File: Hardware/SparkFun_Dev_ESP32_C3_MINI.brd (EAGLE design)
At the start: 21 x 33.3 mm, 88 parts, among them J1 USB Female Type C Connector, J5 Vertical Qwiic Connector, U1 ESP32-C3_MINI-1, U2 RT9080-33GJ5

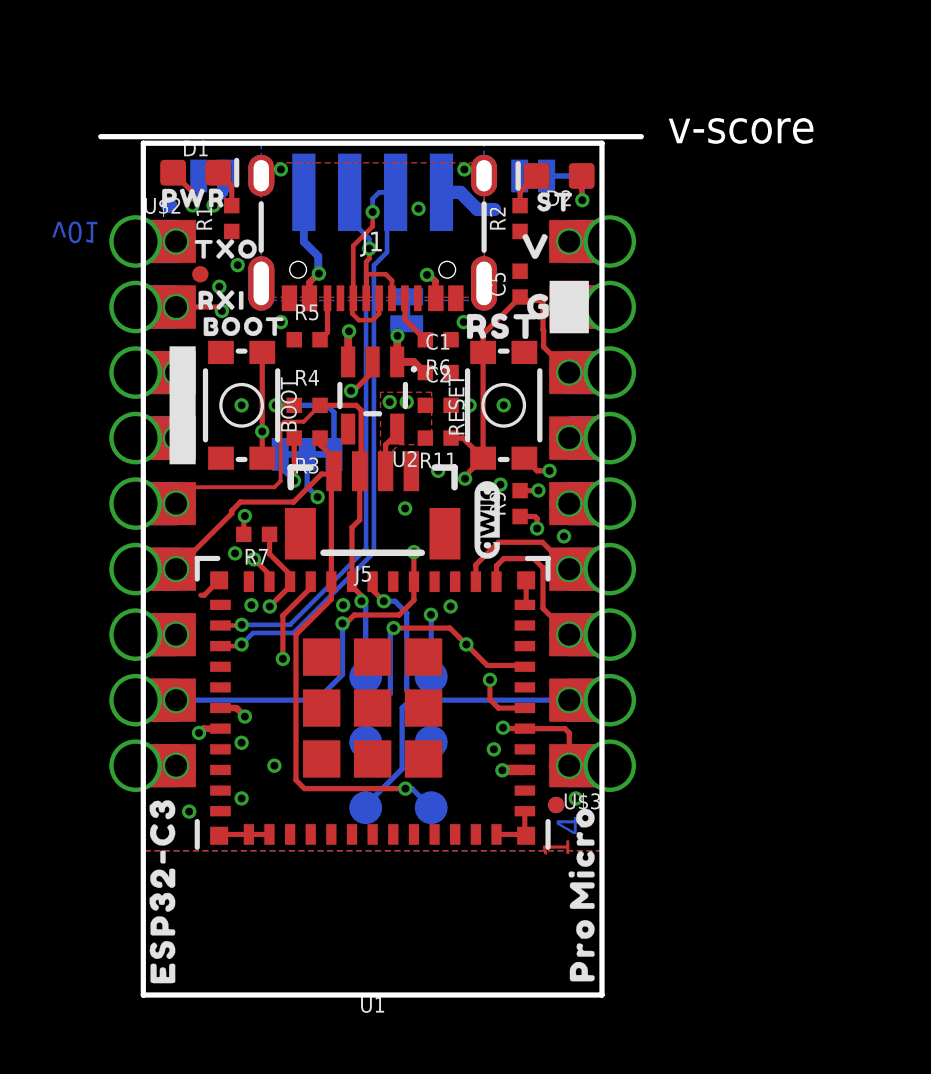
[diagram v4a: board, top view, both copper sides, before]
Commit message: Adds more aesthetic changes
* Note on previous commit: I2C labels were removed from silk
* Fixes ground silk rectangle
* rotates qwiic label
* Shrinks VBUS polygon
* Moves boot capacitor to other side of button
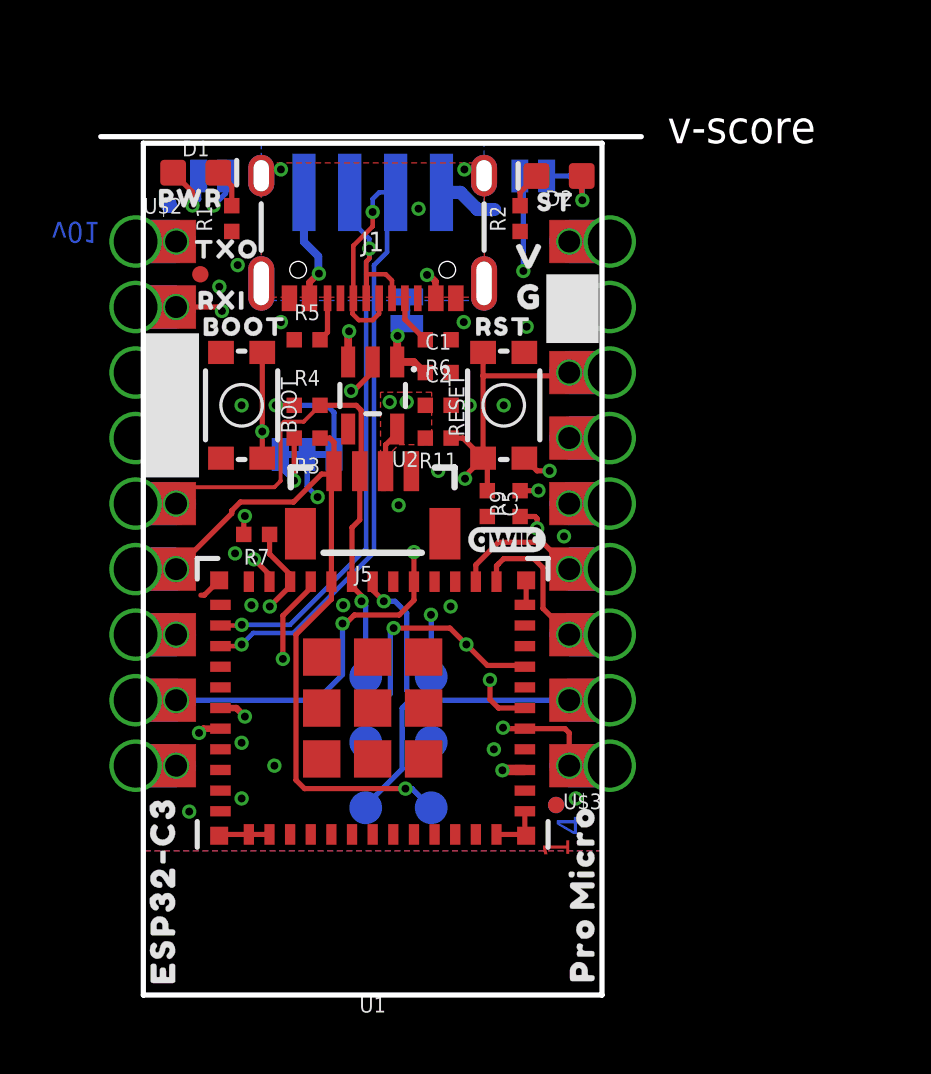
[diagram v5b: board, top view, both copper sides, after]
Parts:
- removed LOGO2: QWIIC_LOGO_3MM, SparkFun-Aesthetics:QWIIC_3MM
- added U$50: (no value), SparkFun-Aesthetics:QWIIC_3MM
- moved C5 8.60 mm to (14.6, 19.1), turned to 270 degrees
- moved U$39 0.54 mm to (16.3, 27.1)
- moved U$38 0.46 mm to (16.3, 28.6)
- moved U$26 0.16 mm to (9.25, 28.6)
- moved U$25 0.13 mm to (11.0, 28.6)
- moved U$44 0.13 mm to (3.10, 30.9)
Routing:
- net IO10/I2S_FS: track 14.5 -> 30.9 mm, vias 2 -> 3
- net !RESET!: track 30.9 -> 28.8 mm
- net GND: vias 21 -> 22

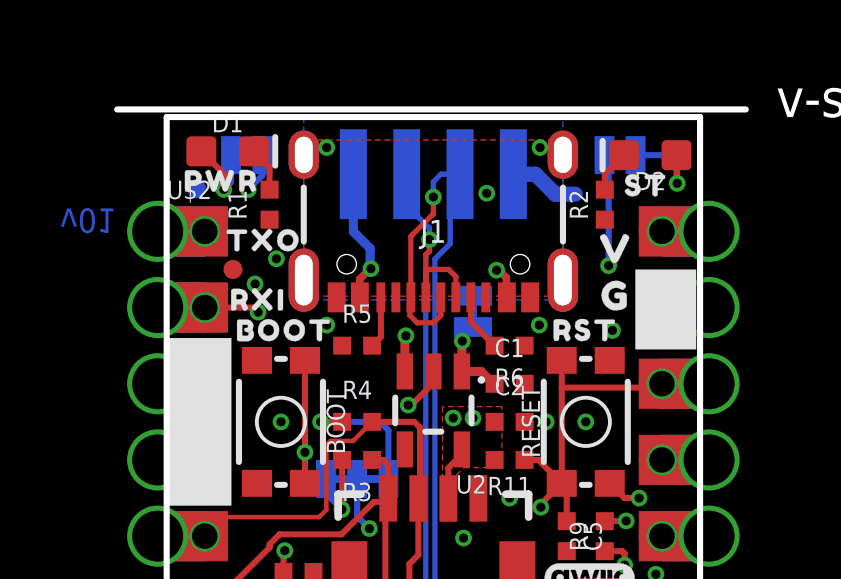
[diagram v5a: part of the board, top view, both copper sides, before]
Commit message: Fixes DRC issues
* Moves shield jumper away from VUSB via
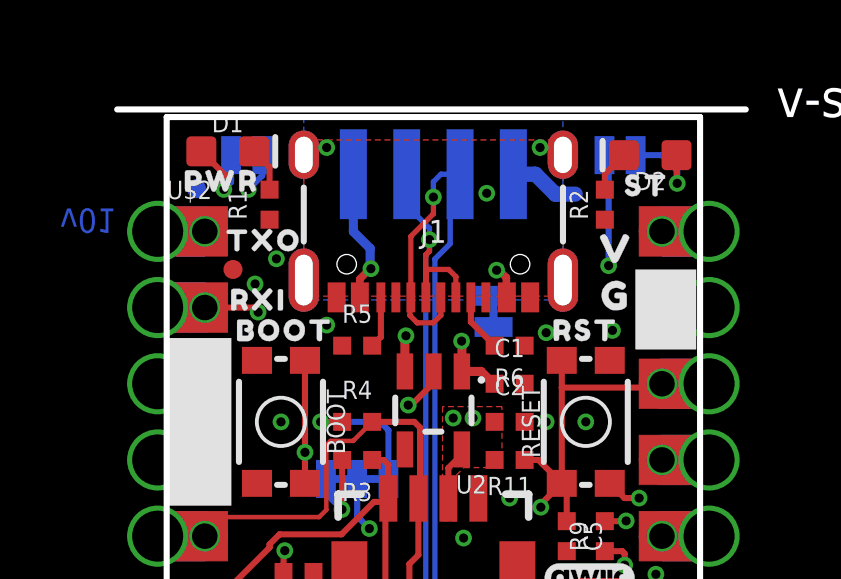
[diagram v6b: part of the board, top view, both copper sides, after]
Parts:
- moved SHLD 0.69 mm to (12.2, 26.5)
- moved U$9 0.60 mm to (14.0, 26.2)
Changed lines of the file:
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@@
 <attribute name="VALUE" x="7.62" y="19.812" size="0.6096" layer="28" font="vector" ratio="20" rot="MR0" align="top-center"/>
 </element>
-<element name="SHLD" library="SparkFun-Jumpers" package="SMT-JUMPER_2_NC_TRACE_SILK" package3d_urn="urn:adsk.eagle:package:39281/1" value="JUMPER-SMT_2_NC_TRACE_SILK" x="11.4808" y="26.543" smashed="yes" rot="MR270">
-<attribute name="NAME" x="10.3378" y="26.543" size="0.6096" layer="26" font="vector" ratio="20" rot="MR270" align="bottom-center"/>
-<attribute name="VALUE" x="12.6238" y="26.543" size="0.6096" layer="28" font="vector" ratio="20" rot="MR270" align="top-center"/>
+<element name="SHLD" library="SparkFun-Jumpers" package="SMT-JUMPER_2_NC_TRACE_SILK" package3d_urn="urn:adsk.eagle:package:39281/1" value="JUMPER-SMT_2_NC_TRACE_SILK" x="12.1666" y="26.543" smashed="yes" rot="MR270">
+<attribute name="NAME" x="11.0236" y="26.543" size="0.6096" layer="26" font="vector" ratio="20" rot="MR270" align="bottom-center"/>
+<attribute name="VALUE" x="13.3096" y="26.543" size="0.6096" layer="28" font="vector" ratio="20" rot="MR270" align="top-center"/>
 </element>
 <element name="R5" library="SparkFun-Resistors" package="0402-TIGHT" value="5.1k" x="7.62" y="25.4" smashed="yes">
@@
 <element name="U$31" library="prod" package="G36" value="" x="12.827" y="28.956" smashed="yes" rot="MR270"/>
 <element name="U$32" library="prod" package="V35" value="" x="7.493" y="28.956" smashed="yes" rot="MR270"/>
-<element name="U$9" library="prod" package="#SH#44" value="" x="13.462" y="26.035" smashed="yes" rot="MR0"/>
+<element name="U$9" library="prod" package="#SH#44" value="" x="14.0462" y="26.1874" smashed="yes" rot="MR0"/>
 <element name="U$33" library="prod" package="G36" value="" x="13.589" y="9.779" smashed="yes" rot="MR0"/>
 <element name="U$34" library="prod" package="ESP32#C32" value="" x="10.16" y="5.08" smashed="yes" rot="MR0"/>
@@
 <wire x1="3.6348" y1="15.5" x2="3.5" y2="15.5" width="0.2" layer="1"/>
 <via x="6.604" y="26.0858" extent="1-16" drill="0.3048"/>
-<via x="13.6906" y="26.0858" extent="1-16" drill="0.3048"/>
+<via x="13.9192" y="25.8318" extent="1-16" drill="0.3048"/>
 <via x="4.2164" y="27.4574" extent="1-16" drill="0.3048"/>
 <via x="18.034" y="7.62" extent="1-16" drill="0.3048"/>
@@
 <vertex x="7.5438" y="27.559"/>
 </polygon>
-<wire x1="11.11" y1="24.5411" x2="11.11" y2="25.5372" width="0.3048" layer="1"/>
-<wire x1="11.11" y1="25.5372" x2="11.1252" y2="25.5524" width="0.3048" layer="1"/>
-<via x="11.1252" y="25.5524" extent="1-16" drill="0.3048"/>
+<wire x1="11.11" y1="24.5411" x2="11.11" y2="25.5422" width="0.3048" layer="1"/>
+<wire x1="11.11" y1="25.5422" x2="11.0998" y2="25.5524" width="0.3048" layer="1"/>
+<via x="11.0998" y="25.5524" extent="1-16" drill="0.3048"/>
 <wire x1="9.21" y1="24.5411" x2="9.21" y2="25.6946" width="0.3048" layer="1"/>
 <wire x1="9.21" y1="25.6946" x2="9.2456" y2="25.7302" width="0.3048" layer="1"/>
@@
 <contactref element="D1" pad="A"/>
 <contactref element="PWR" pad="1"/>
-<wire x1="3.4163" y1="31.75" x2="3.4163" y2="31.3817" width="0.2032" layer="16"/>
 <via x="3.175" y="30.607" extent="1-16" drill="0.3048"/>
 <wire x1="3.175" y1="30.607" x2="3.175" y2="31.127" width="0.2032" layer="1"/>

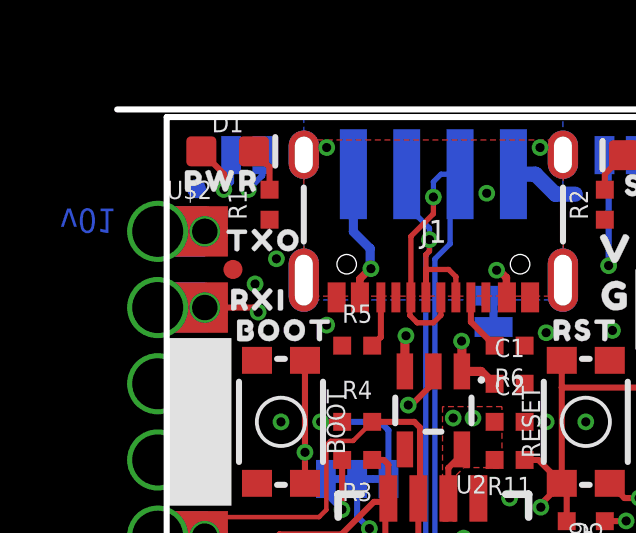
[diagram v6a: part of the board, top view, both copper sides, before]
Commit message: Moves version onto the PCB, and rolls version in schematic
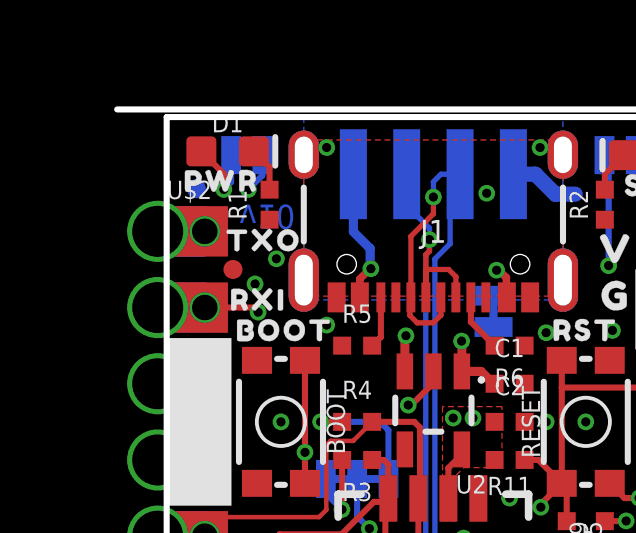
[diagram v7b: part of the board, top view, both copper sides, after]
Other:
- board text added: "v10"
- board text removed: "v01"
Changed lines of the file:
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@@
 <setting verticaltext="up"/>
 </settings>
-<grid distance="0.05" unitdist="inch" unit="inch" style="dots" multiple="1" display="yes" altdistance="0.001" altunitdist="inch" altunit="inch"/>
+<grid distance="0.05" unitdist="inch" unit="inch" style="dots" multiple="1" display="yes" altdistance="0.005" altunitdist="inch" altunit="inch"/>
 <layers>
 <layer number="1" name="Top" color="4" fill="1" visible="yes" active="yes"/>
@@
 <dimension x1="15.24" y1="22.86" x2="19.05" y2="22.86" x3="17.145" y3="36.449" textsize="1.016" textratio="15" layer="47" unit="inch"/>
 <dimension x1="5.08" y1="22.86" x2="1.27" y2="22.86" x3="3.175" y3="36.449" textsize="0.9652" textratio="15" layer="47" unit="inch"/>
-<text x="-2.286" y="29.972" size="0.8128" layer="16" font="vector" ratio="20" rot="SMR180">v01</text>
+<text x="3.683" y="30.099" size="0.8128" layer="16" font="vector" ratio="20" rot="SMR180">v10</text>
 <wire x1="-0.381" y1="33.274" x2="20.574" y2="33.274" width="0.2032" layer="46"/>
 <text x="21.59" y="33.02" size="1.27" layer="46" font="vector" ratio="15">v-score</text>
@@
 <element name="FRAME2" library="SparkFun-Aesthetics" package="CREATIVE_COMMONS" value="FRAME-LEDGER" x="-11.43" y="-25.4" smashed="yes">
 <attribute name="DESIGNER" value="Elias Santistevan" x="-11.43" y="-25.4" size="1.778" layer="27" font="vector" ratio="15" display="off"/>
-<attribute name="REV" value="v01" x="-11.43" y="-25.4" size="1.778" layer="27" font="vector" ratio="15" display="off"/>
+<attribute name="REV" value="v10" x="-11.43" y="-25.4" size="1.778" layer="27" font="vector" ratio="15" display="off"/>
 </element>
 <element name="D2" library="SparkFun-LED" package="LED-0603" value="Blue" x="17.387" y="31.75" smashed="yes" rot="R180">

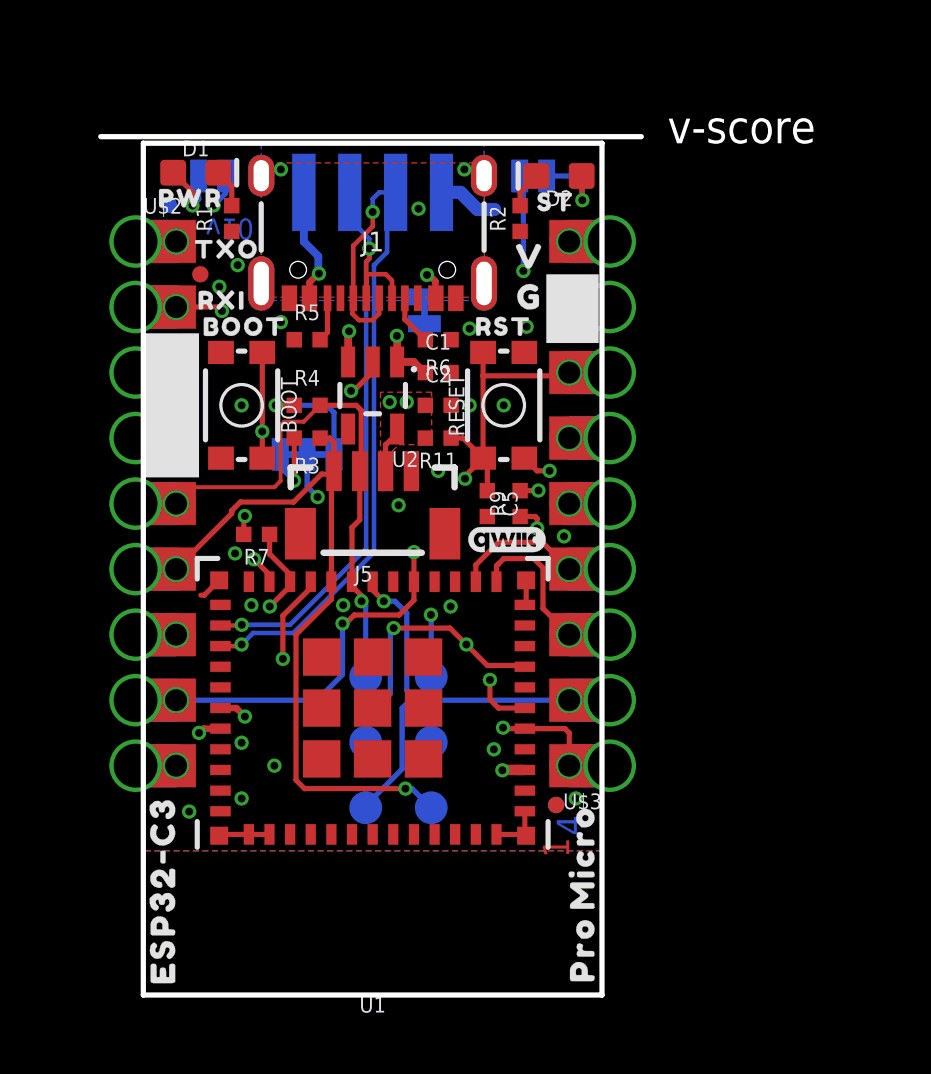
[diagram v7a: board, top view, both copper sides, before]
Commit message: Fixes some acid traps, fixes some schematic odds and ends
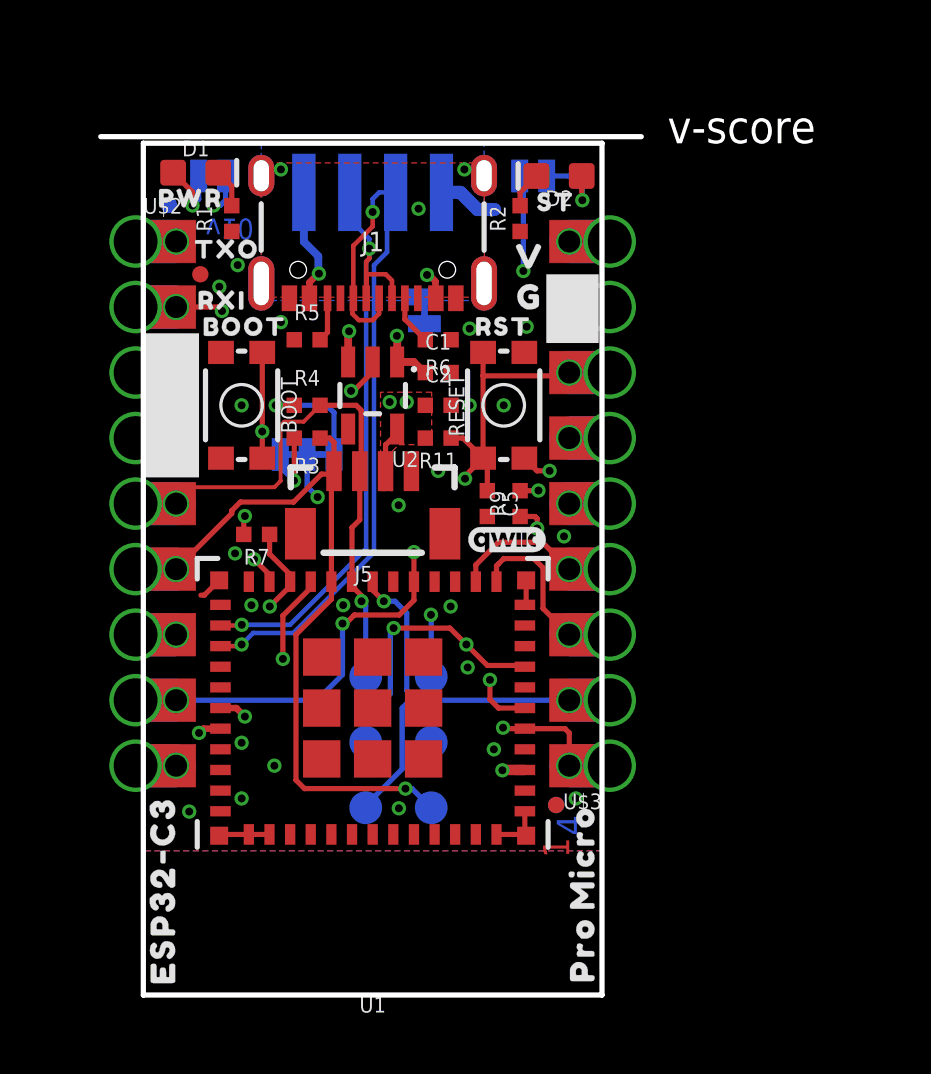
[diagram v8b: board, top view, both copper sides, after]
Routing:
- net GND: vias 22 -> 24
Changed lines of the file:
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@@
 <layer number="45" name="Holes" color="7" fill="1" visible="yes" active="yes"/>
 <layer number="46" name="Milling" color="3" fill="1" visible="no" active="yes"/>
-<layer number="47" name="Measures" color="7" fill="1" visible="no" active="yes"/>
+<layer number="47" name="Measures" color="7" fill="1" visible="yes" active="yes"/>
 <layer number="48" name="Document" color="7" fill="1" visible="no" active="yes"/>
 <layer number="49" name="Reference" color="13" fill="1" visible="yes" active="yes"/>
@@
 <wire x1="7.62" y1="19.7104" x2="8.0264" y2="19.304" width="0.2032" layer="16"/>
 <via x="8.0264" y="19.304" extent="1-16" drill="0.3048"/>
-<wire x1="4.4577" y1="31.75" x2="4.4577" y2="31.0721" width="0.2032" layer="16"/>
-<wire x1="4.4577" y1="31.0721" x2="3.9926" y2="30.607" width="0.2032" layer="16"/>
+<wire x1="4.4577" y1="31.75" x2="4.4577" y2="30.8181" width="0.2032" layer="16"/>
+<wire x1="4.4577" y1="30.8181" x2="4.2466" y2="30.607" width="0.2032" layer="16"/>
+<wire x1="4.2466" y1="30.607" x2="3.9926" y2="30.607" width="0.2032" layer="16"/>
 <via x="3.9926" y="30.607" extent="1-16" drill="0.3048"/>
 </signal>
@@
 <wire x1="16.53" y1="20.32" x2="17.018" y2="20.32" width="0.2032" layer="1"/>
 <via x="16.129" y="25.908" extent="1-16" drill="0.3048"/>
+<via x="11.176" y="7.239" extent="1-16" drill="0.3048"/>
+<via x="13.843" y="12.7" extent="1-16" drill="0.3048"/>
 </signal>
 <signal name="N$4">
@@
 <wire x1="7.493" y1="31.115" x2="7.493" y2="29.19959375" width="0.3048" layer="16"/>
 <wire x1="7.493" y1="29.19959375" x2="8.0522" y2="28.64039375" width="0.3048" layer="16"/>
-<wire x1="17.78" y1="29.21" x2="12.192" y2="29.21" width="0.508" layer="2"/>
-<wire x1="12.192" y1="29.21" x2="10.922" y2="27.94" width="0.508" layer="2"/>
+<wire x1="11.43" y1="28.956" x2="11.43" y2="28.067" width="0.508" layer="2"/>
+<wire x1="17.78" y1="29.21" x2="11.684" y2="29.21" width="0.508" layer="2"/>
+<wire x1="11.684" y1="29.21" x2="11.43" y2="28.956" width="0.508" layer="2"/>
 <wire x1="17.78" y1="29.21" x2="19.35" y2="29.21" width="0" layer="19" extent="1-1"/>
+<wire x1="12.2678" y1="27.9146" x2="11.43" y2="28.067" width="0" layer="19" extent="1-2"/>
+<wire x1="11.0998" y1="25.5524" x2="12.61" y2="27.01" width="0" layer="19" extent="1-1"/>
+<wire x1="9.2456" y1="25.7302" x2="11.0998" y2="25.5524" width="0" layer="19" extent="1-1"/>
+<wire x1="7.71" y1="27.01" x2="9.2456" y2="25.7302" width="0" layer="19" extent="1-1"/>
 </signal>
 <signal name="!RESET!">
